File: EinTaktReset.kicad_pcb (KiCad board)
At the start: 2 copper layers, 100 x 160 mm, 59 parts, among them IC1 74LS624, J1 3PinTerminalBlocktg, J2 3PinTerminalBlocktg, J3 2PinTerminalBlocktg, J4 3PinTerminalBlocktg, J5 2PinTerminalBlocktg, P1 CONN_02X10, P4 CONN_02X10, SW1 SWITCH_INV, SW10 SPST, SW11 SPST, SW12 SPST, SW13 SPST, SW2 SWITCH_INV, SW3 SPST, SW4 SPST, SW5 SPST, SW6 SWITCH_INV, SW7 SPST, SW8 SPST, SW9 SPST, U1 74LS132, U2 74540En, U3 74HCT541_PWR, U4 74LS32, U5 74LS00

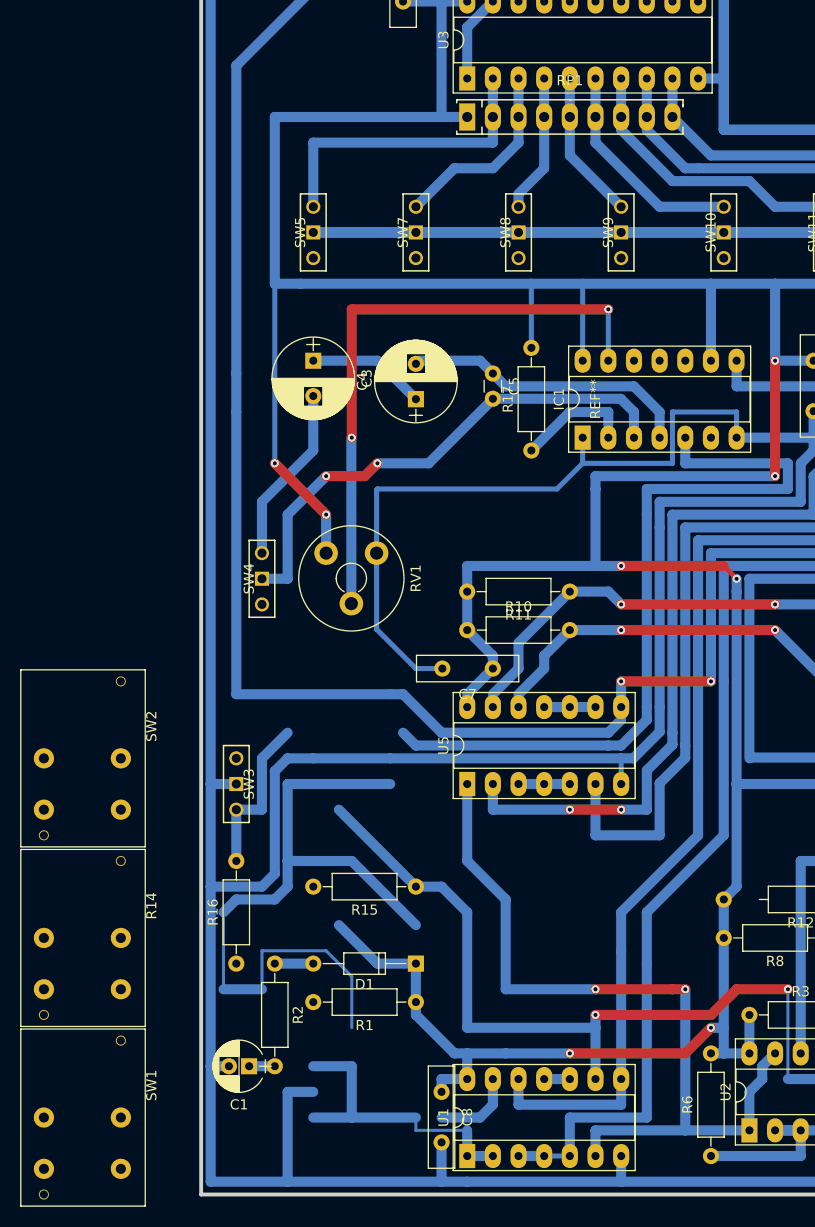
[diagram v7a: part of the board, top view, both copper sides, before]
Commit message: Eintakt Buttons changed
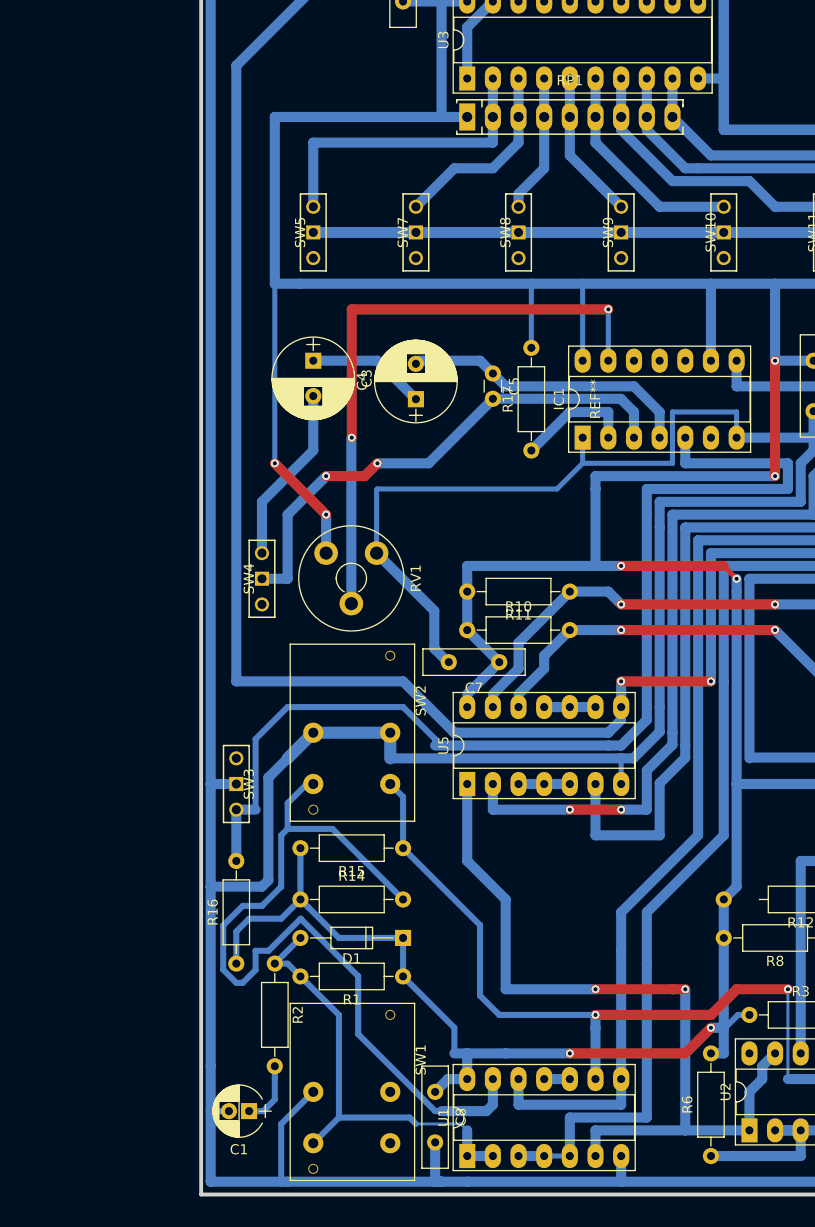
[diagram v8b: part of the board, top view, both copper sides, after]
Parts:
- R14: footprint tg_foodprint:SW_PUSH_LCD_E3_SAxxxx_tg_V2 -> tg_bonsai_proj_spec_libs:R_Axial_DIN0207_L6.3mm_D2.5mm_P10.16mm_Horizontal
- R15: footprint Resistors_ThroughHole:R_Axial_DIN0207_L6.3mm_D2.5mm_P10.16mm_Horizontal -> tg_bonsai_proj_spec_libs:R_Axial_DIN0207_L6.3mm_D2.5mm_P10.16mm_Horizontal
- moved SW1 26.8 mm to (64.8, 176.5)
- moved SW2 26.8 mm to (64.8, 141.0)
- moved R14 18.2 mm to (55.9, 157.5), turned to 0 degrees
- moved C1 4.44 mm to (50.8, 178.4)
- moved R15 4.02 mm to (66.0, 152.4)
- moved D1 2.84 mm to (66.0, 161.3)
- moved R1 2.84 mm to (66.0, 165.1)
- moved C7 0.90 mm to (75.6, 134.0)
- moved C8 0.63 mm to (69.2, 176.5)
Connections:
- SW1 pad 2: Net-(SW1-Pad2) -> (no net)
- U2 pad 20: VCC -> (no net)
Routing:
- net VCC: track 605.8 -> 624.5 mm
- net Net-(IC1-Pad5): track 94.1 -> 109.1 mm
- net Net-(D1-Pad2): track 34.3 -> 44.1 mm
- net Net-(R15-Pad1): track 91.4 -> 87.2 mm
- net Net-(C1-Pad1): track 2.54 -> 6.32 mm
- net Net-(R14-Pad2): track 81.5 -> 82.9 mm
- net GND: track 1112.7 -> 1113.8 mm
- net Net-(U3-Pad1): track 198.4 -> 197.6 mm
